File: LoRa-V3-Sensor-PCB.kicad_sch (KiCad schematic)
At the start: 6 parts, among them IC1 BME690, IC2 SHT40-BD1B-R2, IC3 TSL25911FN

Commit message: remove unwanted fields
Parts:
- IC1: footprint 1projectfootprints:BME68X -> thisProjectLibrary:Bosch_BME680; digikeyPartNumber 828-1077-1-ND -> (none); manufacturerPartNumber BME680 -> BME690; mouserPartNumber 262-BME680 -> (none); octopartUrl https://octopart.com/bme680-bosch+tools-84623084?r=sp -> (none)
- IC2: footprint 1projectfootprints:SHT4X -> 1projectLibrary:SHT4X; mouserPartNumber 403-SHT40-AD1F-R2 -> (none)
- IC3: footprint 1projectfootprints:TSL2591 -> 1GlobalFootprintsLibrary:TSL2591; digikeyPartNumber TSL25911FNCT-ND -> (none); mouserPartNumber 985-TSL25911FN -> (none)
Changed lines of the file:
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@@
 			)
 		)
-		(property "Footprint" "1projectfootprints:SHT4X"
+		(property "Footprint" "1projectLibrary:SHT4X"
 			(at 153.67 140.97 0)
 			(effects
@@
 		(property "manufacturerPartNumber" "SHT40-BD1B-R2"
 			(at 153.67 133.35 0)
-			(effects
-				(font
-					(size 1.27 1.27)
-				)
-				(hide yes)
-			)
-		)
-		(property "mouserPartNumber" "403-SHT40-AD1F-R2"
-			(at 153.67 129.54 0)
 			(effects
 				(font
@@
 			)
 		)
-		(property "Footprint" "1projectfootprints:TSL2591"
+		(property "Footprint" "1GlobalFootprintsLibrary:TSL2591"
 			(at 180.34 129.54 0)
 			(effects
@@
 		(property "manufacturerPartNumber" "TSL25911FN"
 			(at 180.34 135.89 0)
-			(effects
-				(font
-					(size 1.27 1.27)
-				)
-				(hide yes)
-			)
-		)
-		(property "mouserPartNumber" "985-TSL25911FN"
-			(at 180.34 142.24 0)
-			(effects
-				(font
-					(size 1.27 1.27)
-				)
-				(hide yes)
-			)
-		)
-		(property "digikeyPartNumber" "TSL25911FNCT-ND"
-			(at 180.34 138.43 0)
 			(effects
 				(font
@@
 			)
 		)
-		(property "Footprint" "1projectfootprints:BME68X"
+		(property "Footprint" "thisProjectLibrary:Bosch_BME680"
 			(at 163.83 121.92 0)
 			(effects
@@
 			)
 		)
-		(property "octopartUrl" "https://octopart.com/bme680-bosch+tools-84623084?r=sp"
-			(at 127 110.49 0)
-			(effects
-				(font
-					(size 1.27 1.27)
-				)
-				(hide yes)
-			)
-		)
-		(property "manufacturerPartNumber" "BME680"
+		(property "manufacturerPartNumber" "BME690"
 			(at 127 64.77 0)
 			(effects
 				(font
-					(size 1.27 1.27)
-				)
-				(hide yes)
-			)
-		)
-		(property "mouserPartNumber" "262-BME680"
-			(at 127 69.85 0)
-			(effects
-				(font
-					(size 1.27 1.27)
-				)
-				(hide yes)
-			)
-		)
-		(property "digikeyPartNumber" "828-1077-1-ND"
-			(at 125.73 62.23 0)
-			(effects
-				(font

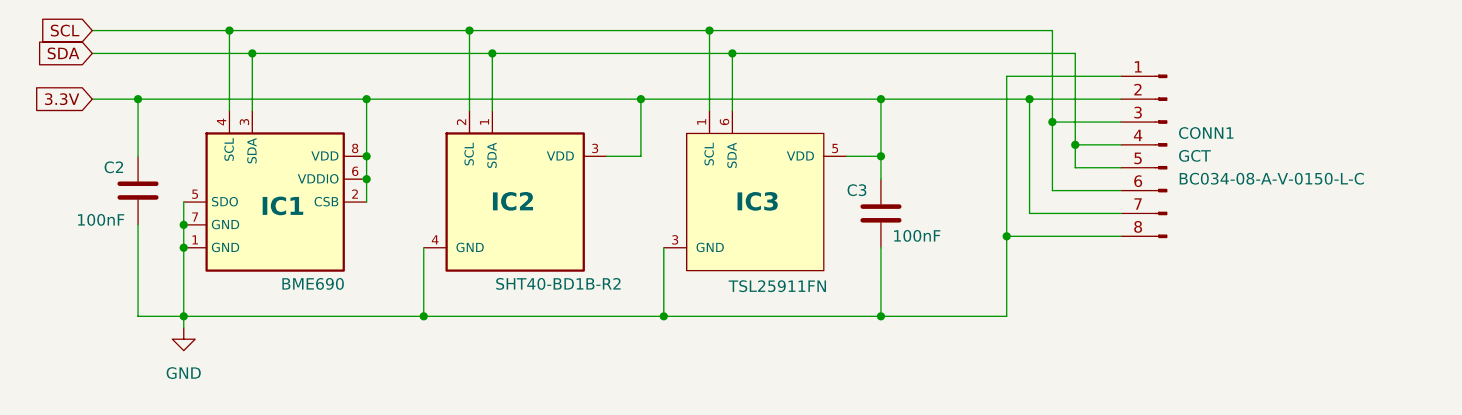
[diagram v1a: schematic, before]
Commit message: change BME680 to 690
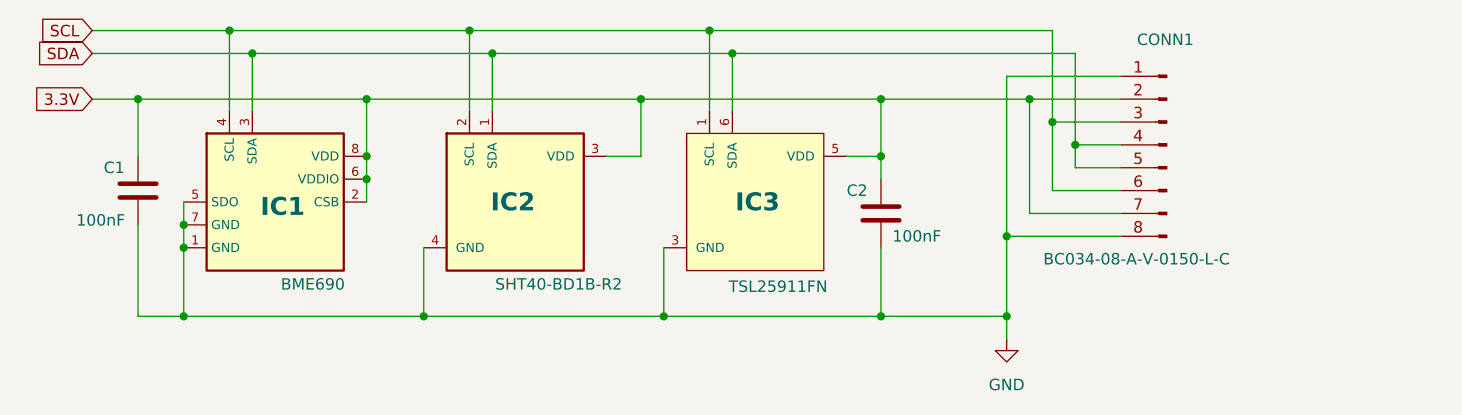
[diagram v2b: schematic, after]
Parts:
- IC1: footprint thisProjectLibrary:Bosch_BME680 -> 1projectfootprints:BME68X; symbol 1projectsymbols:BME680 -> 1projectsymbols:BME690
- IC2: footprint 1projectLibrary:SHT4X -> 1projectfootprints:SHT4X
- IC3: footprint 1GlobalFootprintsLibrary:TSL2591 -> 1projectfootprints:TSL2591
- renumbered C2 to C1, C3 to C2
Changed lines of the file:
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@@
+	)
+	(junction
+		(at 208.28 123.19)
+		(diameter 0)
+		(color 0 0 0 0)
 	)
 	(junction
@@
 	(wire
 		(pts
-			(xy 116.84 124.46) (xy 116.84 123.19)
+			(xy 208.28 125.73) (xy 208.28 123.19)
 		)
 		(stroke
@@
 	(wire
 		(pts
+			(xy 151.13 93.98) (xy 177.8 93.98)
+		)
+		(stroke
+			(width 0)
+			(type default)
+		)
+	)
+	(wire
+		(pts
+			(xy 121.92 91.44) (xy 148.59 91.44)
+		)
+		(stroke
+			(width 0)
+			(type default)
+		)
+	)
+	(wire
+		(pts
+			(xy 111.76 113.03) (xy 111.76 123.19)
+		)
+		(stroke
+			(width 0)
+			(type default)
+		)
+	)
+	(wire
+		(pts
+			(xy 210.82 99.06) (xy 194.31 99.06)
+		)
+		(stroke
+			(width 0)
+			(type default)
+		)
+	)
+	(wire
+		(pts
 			(xy 208.28 123.19) (xy 194.31 123.19)
-		)
-		(stroke
-			(width 0)
-			(type default)
-		)
-	)
-	(wire
-		(pts
-			(xy 151.13 93.98) (xy 177.8 93.98)
-		)
-		(stroke
-			(width 0)
-			(type default)
-		)
-	)
-	(wire
-		(pts
-			(xy 121.92 91.44) (xy 148.59 91.44)
-		)
-		(stroke
-			(width 0)
-			(type default)
-		)
-	)
-	(wire
-		(pts
-			(xy 111.76 113.03) (xy 111.76 123.19)
-		)
-		(stroke
-			(width 0)
-			(type default)
-		)
-	)
-	(wire
-		(pts
-			(xy 210.82 99.06) (xy 194.31 99.06)
 		)
 		(stroke
@@
 			)
 		)
-		(property "Footprint" "1projectLibrary:SHT4X"
+		(property "Footprint" "1projectfootprints:SHT4X"
 			(at 153.67 140.97 0)
 			(effects
@@
 		(on_board yes)
 		(dnp no)
-		(property "Reference" "C3"
+		(property "Reference" "C2"
 			(at 190.5 109.22 0)
 			(effects
@@
 			(project "LoRa-V3-Sensor-PCB"
 				(path "/cdafba45-6306-47c3-b944-cdbdf8a9c0e4"
-					(reference "C3")
+					(reference "C2")
 					(unit 1)
 				)
@@
 		(on_board yes)
 		(dnp no)
-		(property "Reference" "C2"
+		(property "Reference" "C1"
 			(at 107.95 106.68 0)
 			(effects
@@
 			(project "LoRa-V3-Sensor-PCB"
 				(path "/cdafba45-6306-47c3-b944-cdbdf8a9c0e4"
-					(reference "C2")
+					(reference "C1")
 					(unit 1)
 				)
@@
 		(on_board yes)
 		(dnp no)
-		(fields_autoplaced yes)
 		(property "Reference" "CONN1"
-			(at 227.33 102.8699 0)
+			(at 222.758 92.456 0)
 			(effects
 				(font
@@
 		)
 		(property "manufacturerName" "GCT"
-			(at 227.33 105.4099 0)
+			(at 219.964 116.586 0)
 			(effects
 				(font
@@
 				)
 				(justify right)
+				(hide yes)
 			)
 		)
 		(property "manufacturerPartNumber" "BC034-08-A-V-0150-L-C"
-			(at 227.33 107.9499 0)
+			(at 212.344 116.84 0)
 			(effects
 				(font
@@
 			)
 		)
-		(property "Footprint" "1GlobalFootprintsLibrary:TSL2591"
+		(property "Footprint" "1projectfootprints:TSL2591"
 			(at 180.34 129.54 0)
 			(effects
@@
 	)
 	(symbol
-		(lib_id "1projectsymbols:BME680")
+		(lib_id "1projectsymbols:BME690")
 		(at 127 110.49 0)
 		(unit 1)
@@
 			)
 		)
-		(property "Footprint" "thisProjectLibrary:Bosch_BME680"
+		(property "Footprint" "1projectfootprints:BME68X"
 			(at 163.83 121.92 0)
 			(effects
@@
 	(symbol
 		(lib_id "power:GND")
-		(at 116.84 124.46 0)
+		(at 208.28 125.73 0)
 		(unit 1)
 		(exclude_from_sim no)
@@
 		(fields_autoplaced yes)
 		(property "Reference" "#PWR01"
-			(at 116.84 130.81 0)
+			(at 208.28 132.08 0)
 			(effects
 				(font
@@
 		)
 		(property "Value" "GND"
-			(at 116.84 129.54 0)
+			(at 208.28 130.81 0)
 			(effects
 				(font
@@
 		)
 		(property "Footprint" ""
-			(at 116.84 124.46 0)
+			(at 208.28 125.73 0)
 			(effects
 				(font
@@
 		)
 		(property "Datasheet" ""
-			(at 116.84 124.46 0)
+			(at 208.28 125.73 0)
 			(effects
 				(font
@@
 		)
 		(property "Description" "Power symbol creates a global label with name \"GND\" , ground"
-			(at 116.84 124.46 0)
-			(effects
-				(font
+			(at 208.28 125.73 0)
+			(effects
+				(font

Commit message: move ic3 to back side
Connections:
- net SCL: now also CONN1.4 (SDA), CONN1.5 (SDA); no longer CONN1.3 (SCL), CONN1.6 (SCL)
- net SDA: now also CONN1.3 (SCL), CONN1.6 (SCL); no longer CONN1.4 (SDA), CONN1.5 (SDA)
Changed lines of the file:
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@@
+	)
+	(junction
+		(at 167.64 99.06)
+		(diameter 0)
+		(color 0 0 0 0)
+	)
+	(junction
+		(at 148.59 91.44)
+		(diameter 0)
+		(color 0 0 0 0)
+	)
+	(junction
+		(at 177.8 93.98)
+		(diameter 0)
+		(color 0 0 0 0)
+	)
+	(junction
+		(at 194.31 99.06)
+		(diameter 0)
+		(color 0 0 0 0)
+	)
+	(junction
+		(at 210.82 99.06)
+		(diameter 0)
+		(color 0 0 0 0)
+	)
+	(junction
+		(at 170.18 123.19)
+		(diameter 0)
+		(color 0 0 0 0)
 	)
 	(junction
@@
 	)
 	(junction
-		(at 167.64 99.06)
-		(diameter 0)
-		(color 0 0 0 0)
-	)
-	(junction
-		(at 148.59 91.44)
-		(diameter 0)
-		(color 0 0 0 0)
-	)
-	(junction
-		(at 177.8 93.98)
-		(diameter 0)
-		(color 0 0 0 0)
-	)
-	(junction
-		(at 194.31 99.06)
-		(diameter 0)
-		(color 0 0 0 0)
-	)
-	(junction
-		(at 210.82 99.06)
-		(diameter 0)
-		(color 0 0 0 0)
-	)
-	(junction
-		(at 170.18 123.19)
-		(diameter 0)
-		(color 0 0 0 0)
-	)
-	(junction
 		(at 143.51 123.19)
 		(diameter 0)
@@
 	)
 	(junction
+		(at 208.28 114.3)
+		(diameter 0)
+		(color 0 0 0 0)
+	)
+	(junction
+		(at 111.76 99.06)
+		(diameter 0)
+		(color 0 0 0 0)
+	)
+	(junction
+		(at 116.84 115.57)
+		(diameter 0)
+		(color 0 0 0 0)
+	)
+	(junction
+		(at 194.31 123.19)
+		(diameter 0)
+		(color 0 0 0 0)
+	)
+	(junction
+		(at 121.92 91.44)
+		(diameter 0)
+		(color 0 0 0 0)
+	)
+	(junction
+		(at 194.31 105.41)
+		(diameter 0)
+		(color 0 0 0 0)
+	)
+	(junction
+		(at 137.16 107.95)
+		(diameter 0)
+		(color 0 0 0 0)
+	)
+	(junction
 		(at 213.36 101.6)
 		(diameter 0)
 		(color 0 0 0 0)
 	)
-	(junction
-		(at 208.28 114.3)
-		(diameter 0)
-		(color 0 0 0 0)
-	)
-	(junction
-		(at 111.76 99.06)
-		(diameter 0)
-		(color 0 0 0 0)
-	)
-	(junction
-		(at 116.84 115.57)
-		(diameter 0)
-		(color 0 0 0 0)
-	)
-	(junction
-		(at 194.31 123.19)
-		(diameter 0)
-		(color 0 0 0 0)
-	)
-	(junction
-		(at 121.92 91.44)
-		(diameter 0)
-		(color 0 0 0 0)
-	)
-	(junction
-		(at 194.31 105.41)
-		(diameter 0)
-		(color 0 0 0 0)
-	)
-	(junction
-		(at 137.16 107.95)
-		(diameter 0)
-		(color 0 0 0 0)
-	)
 	(wire
 		(pts
@@
 	(wire
 		(pts
+			(xy 213.36 93.98) (xy 213.36 101.6)
+		)
+		(stroke
+			(width 0)
+			(type default)
+		)
+	)
+	(wire
+		(pts
 			(xy 220.98 96.52) (xy 208.28 96.52)
 		)
@@
 	(wire
 		(pts
-			(xy 177.8 93.98) (xy 215.9 93.98)
+			(xy 177.8 93.98) (xy 213.36 93.98)
 		)
 		(stroke
@@
 	(wire
 		(pts
-			(xy 213.36 91.44) (xy 213.36 101.6)
-		)
-		(stroke
-			(width 0)
-			(type default)
-		)
-	)
-	(wire
-		(pts
 			(xy 106.68 93.98) (xy 124.46 93.98)
 		)
@@
 	(wire
 		(pts
-			(xy 175.26 91.44) (xy 213.36 91.44)
+			(xy 175.26 91.44) (xy 215.9 91.44)
 		)
 		(stroke
@@
 	(wire
 		(pts
+			(xy 215.9 91.44) (xy 215.9 104.14)
+		)
+		(stroke
+			(width 0)
+			(type default)
+		)
+	)
+	(wire
+		(pts
 			(xy 194.31 99.06) (xy 167.64 99.06)
 		)
@@
 		)
 		(stroke
-			(width 0)
-			(type default)
-		)
-	)
-	(wire
-		(pts
-			(xy 215.9 93.98) (xy 215.9 104.14)
-		)
-		(stroke
